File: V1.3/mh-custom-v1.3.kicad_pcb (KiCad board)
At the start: 2 copper layers, 93 x 91.3 mm, 118 parts, among them J1 Conn_01x03_Male, J10 Screw_Terminal_01x02, J11 Screw_Terminal_01x02, J12 Screw_Terminal_01x02, J13 USB_A, J14 Screw_Terminal_01x02, J15 Conn_02x16_Row_Letter_Last, J16 Conn_02x12_Row_Letter_Last, J5 Screw_Terminal_01x02, J6 Screw_Terminal_01x02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

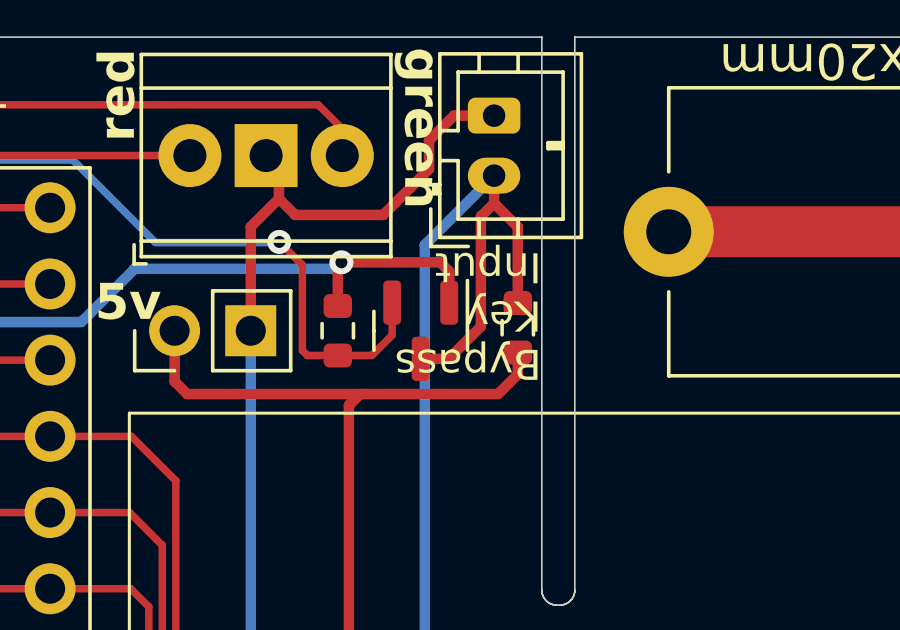
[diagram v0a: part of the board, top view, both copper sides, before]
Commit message: moved bypass key and led labels
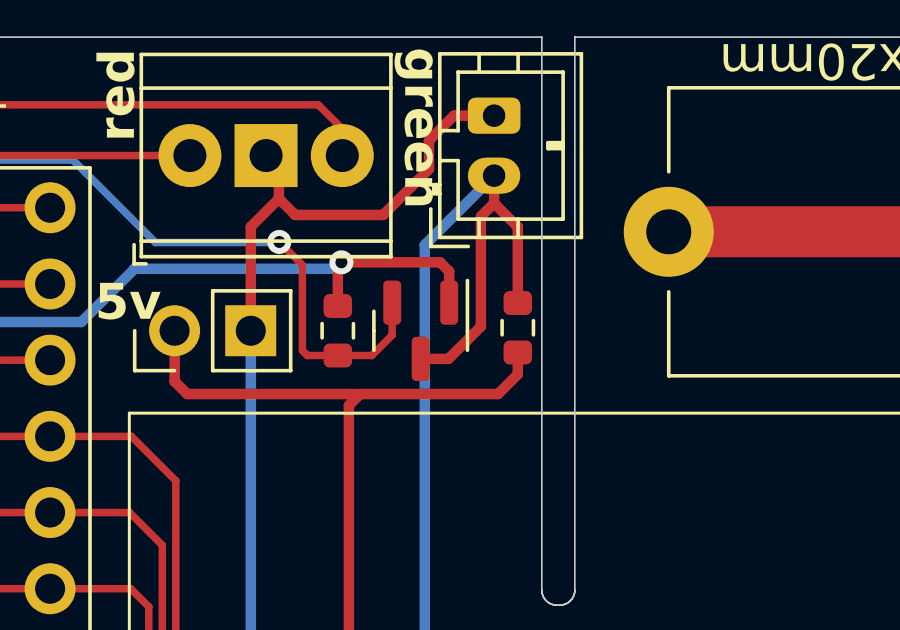
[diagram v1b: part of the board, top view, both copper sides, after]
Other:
- board text added: "R/G LED"
- board text added: "key"
- board text removed: "Bypass Key Input"
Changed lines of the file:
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@@
 		)
 	)
+	(gr_text "R/G LED"
+		(at 67.695 25.42 0)
+		(layer "B.SilkS")
+		(effects
+			(font
+				(size 1.5 1.5)
+				(thickness 0.3)
+				(bold yes)
+			)
+			(justify left bottom)
+		)
+	)
+	(gr_text "key"
+		(at 79.435 27.33 90)
+		(layer "B.SilkS")
+		(effects
+			(font
+				(size 1.5 1.5)
+				(thickness 0.3)
+				(bold yes)
+			)
+			(justify left bottom)
+		)
+	)
 	(gr_text "3 stages of relays\nFeather [WiFi] microcontroller\n2x E-Stop Integration\nCurrent Sensor"
 		(at 76.015 74.49 90)
@@
 		)
 	)
-	(gr_text "Bypass\nKey\nInput"
-		(at 82.015 32.19 180)
-		(layer "F.SilkS")
-		(effects
-			(font
-				(size 1 1)
-				(thickness 0.15)
-			)
-			(justify left)
-		)
-	)
 	(gr_text "MAX4A Fuses   5x20mm"
 		(at 97.935 23.7 180)
@@
 			"17958945-b4e5-4907-bdac-17ac1be8aeb7" "1eba8193-458a-4f8f-b496-5cd575e28d2e"
 			"21afb476-0163-4237-92db-8edd745e1eea" "22f72e0e-eb98-4883-b6db-5a118503c105"
-			"2550d0ec-683d-4be2-8794-d12b50d0d337" "29513e16-f12e-4352-b04b-dbd367b3c74a"
-			"295b06c7-e252-49b7-8a38-90fc508759aa" "34e09b9a-b600-4ada-8310-7c22730c7a67"
-			"38bfa293-1efc-4a4b-af5c-c6b398314e59" "3aa51f6b-5cfb-430a-a636-70ef1de7403d"
-			"3af1d50f-77a8-4823-b4be-9f8b6ecbdc7f" "3b67650f-9d43-435d-a4cb-f2b5c7b001b8"
-			"3e743c7e-5ef6-4c2b-9c4e-ca277ca6c139" "408bff59-9e59-4f04-9da1-94cdd9e4103e"
-			"414d6d0b-ebf2-4fe3-8636-3efca53d629c" "439b5404-ade4-4f5e-b38e-8e408305b0c5"
-			"465002d1-5889-45b8-a6e7-8e887e534c1e" "492cf508-daab-4356-a38d-12ad1886da1f"
-			"50597134-2ed5-408f-a813-e2581a61d251" "5698626b-8952-45af-bb77-57279943d3eb"
-			"584212ba-44d1-45a4-bfd9-fdcf5eec124d" "590466cf-07d7-4fb1-b0d5-cbfa69c59bae"
-			"59d04f74-5c65-460f-b996-c2b3a4ebb9fb" "5a2e864c-16e6-40d4-acce-bcec9eb9347b"
-			"5b481577-4d0c-4c9c-b396-abc133042409" "6134f302-f9a9-4cd2-8eea-1ba168d35a78"
-			"62588a2d-fa92-4e05-ae38-b68466984832" "6c0ca485-d34e-470e-98bc-fbc74fdcb446"
-			"70326d7e-9b73-4430-bb83-f5fa03c84a4d" "73fe44ca-7166-4dc6-a87e-0772ad8112bc"
-			"78a1b218-8262-40ce-b14f-864e02ac2a92" "82d2c86b-827d-4dae-b0b6-12a0a6e95fc4"
-			"84ab4415-58b5-44fc-a97a-9d447aef33e6" "85f53170-4516-4501-a000-3ba7a9aff425"
-			"87784ff4-fb95-4a61-8c16-4d3351d61679" "8d47d5ad-25f9-428f-900d-75f7e963e3c9"
-			"8e117e59-b2e0-4634-bd48-d223e300b05c" "8eb8abda-5f0b-480b-b9fa-d0bf0bbb88cf"
-			"934da9de-7ab7-41db-b04a-0737f17e9c00" "94d803e1-8cde-45aa-a1dc-5da856157556"
-			"97b0d988-ae48-44f6-b5d7-e3019f3f0008" "9c4cb01b-a57f-45d4-acdb-abd029d172c6"
-			"9d02bc0a-ac59-4ac8-ba2a-c8af13b700e9" "9f149bd0-1082-4a7f-8192-95bd0183291d"
-			"a360a2a5-503b-4e7b-ade7-c66933740494" "a3e29f78-74de-4864-8898-e08405603c39"
-			"a9a19ec2-157e-4fee-91ac-d43c3b62c388" "acae978b-2fc8-4245-a42c-13c7bcd02ae8"
-			"af898ec6-8398-41a1-b0ba-9b606ce959ce" "b1318dab-5955-43c4-ac8c-b5a328f70a44"
-			"b2d13ab4-6efe-4b38-9b5b-f173cdfb8701" "b42c07d1-11fe-4424-b759-0d1276d03285"
-			"b6e41199-3fee-4d47-bd67-1ba33aa292e9" "b925d684-2c76-4e7a-b534-ac7c16bc0ae3"
-			"bc5ed0a8-de7a-4749-a68e-229cd1c0a231" "c1ba262e-6206-4bc8-a9ac-dae23533be60"
-			"c2ac6580-32b8-4e11-a545-ebc8dc801088" "c7707fc4-b28a-4655-8f75-10bdcb199e59"
-			"ca6a5f29-a8e5-45c1-ae70-af50c3a38a07" "cc2fcf3c-85e7-49be-b7bd-3e4b750f2179"
-			"ce898617-f0af-4fd4-b81a-07bd27980ecc" "cf8372bf-3328-4e25-9cf9-8e29cff3b115"
-			"d2b5cae1-5983-4108-8894-ccd4c23e48ee" "d505db84-2666-403b-9e6f-7135ce8c6eaa"
-			"e5543da5-a531-4810-83b5-3e0106f3a2cc" "e56ba5bc-d532-4dd0-a4c4-5f68e814dbc5"
-			"e670ab2b-b84d-45d7-bd66-d3d1c50571f3" "ead11c8b-1ad6-4648-827c-de4dfb5421bd"
-			"edf3f12c-61c8-467c-8d0e-44c0f2bdbe4d" "f7141665-cc66-4778-895e-a5e442e220fc"
-			"fb9e3b5e-7543-43c4-87dc-00f8ad6d4efc" "fd1a9feb-2a32-421e-b513-64c14429d371"
+			"2550d0ec-683d-4be2-8794-d12b50d0d337" "295b06c7-e252-49b7-8a38-90fc508759aa"
+			"34e09b9a-b600-4ada-8310-7c22730c7a67" "38bfa293-1efc-4a4b-af5c-c6b398314e59"
+			"3aa51f6b-5cfb-430a-a636-70ef1de7403d" "3af1d50f-77a8-4823-b4be-9f8b6ecbdc7f"
+			"3b67650f-9d43-435d-a4cb-f2b5c7b001b8" "3e743c7e-5ef6-4c2b-9c4e-ca277ca6c139"
+			"408bff59-9e59-4f04-9da1-94cdd9e4103e" "414d6d0b-ebf2-4fe3-8636-3efca53d629c"
+			"439b5404-ade4-4f5e-b38e-8e408305b0c5" "465002d1-5889-45b8-a6e7-8e887e534c1e"
+			"492cf508-daab-4356-a38d-12ad1886da1f" "50597134-2ed5-408f-a813-e2581a61d251"
+			"5698626b-8952-45af-bb77-57279943d3eb" "584212ba-44d1-45a4-bfd9-fdcf5eec124d"
+			"590466cf-07d7-4fb1-b0d5-cbfa69c59bae" "59d04f74-5c65-460f-b996-c2b3a4ebb9fb"
+			"5a2e864c-16e6-40d4-acce-bcec9eb9347b" "5b481577-4d0c-4c9c-b396-abc133042409"
+			"6134f302-f9a9-4cd2-8eea-1ba168d35a78" "62588a2d-fa92-4e05-ae38-b68466984832"
+			"6c0ca485-d34e-470e-98bc-fbc74fdcb446" "70326d7e-9b73-4430-bb83-f5fa03c84a4d"
+			"73fe44ca-7166-4dc6-a87e-0772ad8112bc" "78a1b218-8262-40ce-b14f-864e02ac2a92"
+			"82d2c86b-827d-4dae-b0b6-12a0a6e95fc4" "84ab4415-58b5-44fc-a97a-9d447aef33e6"
+			"85f53170-4516-4501-a000-3ba7a9aff425" "87784ff4-fb95-4a61-8c16-4d3351d61679"
+			"8d47d5ad-25f9-428f-900d-75f7e963e3c9" "8e117e59-b2e0-4634-bd48-d223e300b05c"
+			"8eb8abda-5f0b-480b-b9fa-d0bf0bbb88cf" "934da9de-7ab7-41db-b04a-0737f17e9c00"
+			"94d803e1-8cde-45aa-a1dc-5da856157556" "97b0d988-ae48-44f6-b5d7-e3019f3f0008"
+			"9c4cb01b-a57f-45d4-acdb-abd029d172c6" "9d02bc0a-ac59-4ac8-ba2a-c8af13b700e9"
+			"9f149bd0-1082-4a7f-8192-95bd0183291d" "a360a2a5-503b-4e7b-ade7-c66933740494"
+			"a3e29f78-74de-4864-8898-e08405603c39" "a9a19ec2-157e-4fee-91ac-d43c3b62c388"
+			"acae978b-2fc8-4245-a42c-13c7bcd02ae8" "af898ec6-8398-41a1-b0ba-9b606ce959ce"
+			"b1318dab-5955-43c4-ac8c-b5a328f70a44" "b2d13ab4-6efe-4b38-9b5b-f173cdfb8701"
+			"b42c07d1-11fe-4424-b759-0d1276d03285" "b6e41199-3fee-4d47-bd67-1ba33aa292e9"
+			"b925d684-2c76-4e7a-b534-ac7c16bc0ae3" "bc5ed0a8-de7a-4749-a68e-229cd1c0a231"
+			"c1ba262e-6206-4bc8-a9ac-dae23533be60" "c2ac6580-32b8-4e11-a545-ebc8dc801088"
+			"c7707fc4-b28a-4655-8f75-10bdcb199e59" "ca6a5f29-a8e5-45c1-ae70-af50c3a38a07"
+			"cc2fcf3c-85e7-49be-b7bd-3e4b750f2179" "ce898617-f0af-4fd4-b81a-07bd27980ecc"
+			"cf8372bf-3328-4e25-9cf9-8e29cff3b115" "d2b5cae1-5983-4108-8894-ccd4c23e48ee"
+			"d505db84-2666-403b-9e6f-7135ce8c6eaa" "e5543da5-a531-4810-83b5-3e0106f3a2cc"
+			"e56ba5bc-d532-4dd0-a4c4-5f68e814dbc5" "e670ab2b-b84d-45d7-bd66-d3d1c50571f3"
+			"ead11c8b-1ad6-4648-827c-de4dfb5421bd" "edf3f12c-61c8-467c-8d0e-44c0f2bdbe4d"
+			"f7141665-cc66-4778-895e-a5e442e220fc" "fb9e3b5e-7543-43c4-87dc-00f8ad6d4efc"
+			"fd1a9feb-2a32-421e-b513-64c14429d371"
 		)
 	)

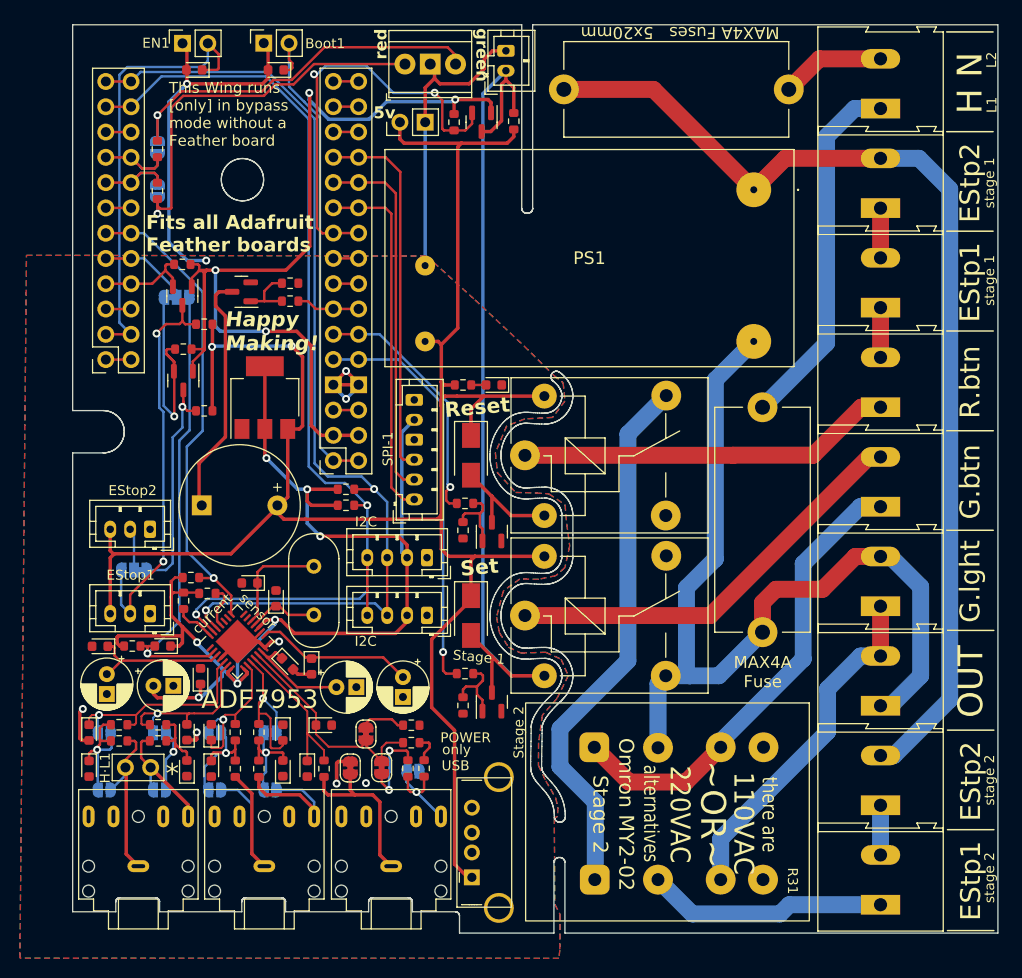
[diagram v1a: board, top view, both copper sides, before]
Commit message: rounded high voltage tracks
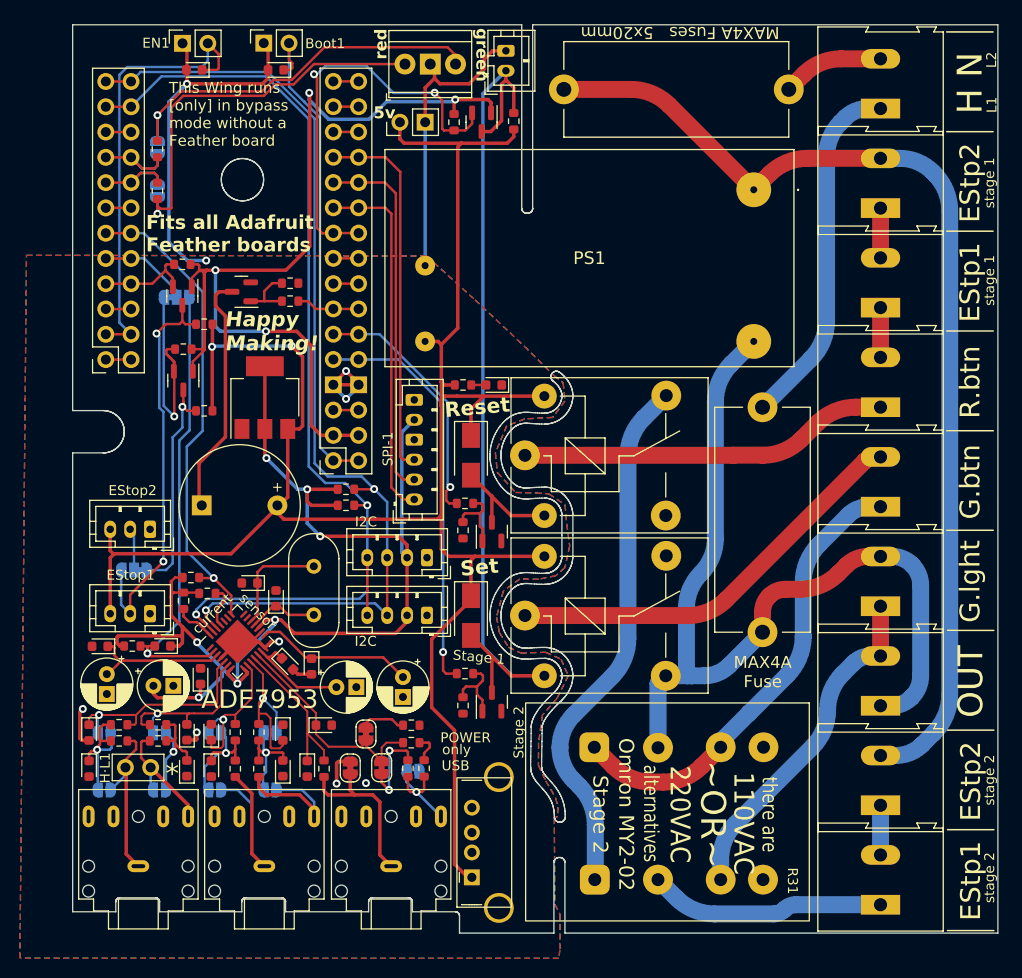
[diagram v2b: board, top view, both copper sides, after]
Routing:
- net reset: track 54.5 -> 53.3 mm
- net Member-Green-Button-2: track 47.6 -> 46.6 mm
- net Green-Indicator-light-2: track 35.3 -> 34.4 mm
- net H/L1: track 36.5 -> 35.8 mm
- net Member-Red-Reset-Button-1: track 37.7 -> 37.2 mm

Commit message: revised some values for interactive BOM
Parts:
- IN-1: value H/L1 -> 3.5mm
- IN-2: value N/L2 -> 3.5mm
- IN-3: value VOLTS -> 3.5mm
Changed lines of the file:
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@@
 			)
 		)
-		(property "Value" "H/L1"
+		(property "Value" "3.5mm"
 			(at 0 -10 0)
 			(layer "F.Fab")
@@
 			)
 		)
-		(property "Value" "N/L2"
+		(property "Value" "3.5mm"
 			(at 0 -10 0)
 			(layer "F.Fab")
@@
 			)
 		)
-		(property "Value" "VOLTS"
+		(property "Value" "3.5mm"
 			(at 0 -10 0)
 			(layer "F.Fab")

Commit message: added interactive Bill of Materials
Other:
- board text added: "5V"
- board text added: "GND"
- board text added: "Use at own risk"
- board text added: "bypass key"
- board text added: "grn"
- board text added: "https://learn.adafruit.com/ adafruit-feather/feather-specification"
- board text added: "status LEDs"
- board text removed: "R/G LED"
- board text removed: "Use at your own risk"
- board text removed: "key"
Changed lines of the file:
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@@
 		(legacy_teardrops no)
 	)
-	(paper "A4")
+	(paper "USLetter")
+	(title_block
+		(title "Cardsystem Combined-Use Feather Wing")
+		(date "2024-03-02")
+		(rev "1.3.1")
+		(company "MakeHaven")
+		(comment 1 "Feather Wing compatable Board")
+		(comment 2 "Primary use: tool control & RFID card reader")
+		(comment 3 "Tool control by onboard multi-stage Relays - powered by input AC voltage")
+		(comment 4 "Add daughter board for RFID card read: I2C intended, but SPI could work as well")
+		(comment 5 "other extensions possible, as specified in Docs")
+	)
 	(layers
 		(0 "F.Cu" signal)
@@
 		(layer "B.SilkS")
 	)
+	(gr_line
+		(start 74.325 33.87)
+		(end 67.705 33.87)
+		(stroke
+			(width 0.15)
+			(type default)
+		)
+		(layer "B.SilkS")
+	)
 	(gr_poly
 		(pts
@@
 		(layer "B.SilkS")
 	)
+	(gr_line
+		(start 74.325 30.55)
+		(end 74.325 33.87)
+		(stroke
+			(width 0.15)
+			(type default)
+		)
+		(layer "B.SilkS")
+	)
 	(gr_poly
 		(pts
@@
 		(layer "B.SilkS")
 	)
+	(gr_line
+		(start 74.325 30.55)
+		(end 67.695 30.55)
+		(stroke
+			(width 0.15)
+			(type default)
+		)
+		(layer "B.SilkS")
+	)
 	(gr_poly
 		(pts
@@
 		(layer "B.SilkS")
 	)
+	(gr_line
+		(start 71.015 33.87)
+		(end 71.01 30.55)
+		(stroke
+			(width 0.15)
+			(type default)
+		)
+		(layer "B.SilkS")
+	)
 	(gr_poly
 		(pts
@@
 	)
 	(gr_line
-		(start 74.873116 30.402956)
-		(end 74.876884 46.197043)
+		(start 38.445 35.65)
+		(end 38.476884 47.517044)
 		(stroke
 			(width 0.15)
@@
 		(layer "B.SilkS")
 	)
+	(gr_line
+		(start 67.695 30.55)
+		(end 67.705 33.87)
+		(stroke
+			(width 0.15)
+			(type default)
+		)
+		(layer "B.SilkS")
+	)
 	(gr_poly
 		(pts
@@
 		)
 	)
-	(gr_text "Use at your own risk"
-		(at 74.175 38.15 90)
+	(gr_text "Use at own risk"
+		(at 37.756884 41.517044 90)
 		(layer "B.SilkS")
 		(effects
@@
 		)
 	)
-	(gr_text "R/G LED"
-		(at 67.695 25.42 0)
+	(gr_text "red"
+		(at 71.425 25.77 0)
 		(layer "B.SilkS")
 		(effects
 			(font
-				(size 1.5 1.5)
-				(thickness 0.3)
-				(bold yes)
+				(size 1 1)
+				(thickness 0.15)
 			)
-			(justify left bottom)
+			(justify left bottom mirror)
 		)
 	)
-	(gr_text "key"
-		(at 79.435 27.33 90)
+	(gr_text "bypass key"
+		(at 79.465 22.81 90)
 		(layer "B.SilkS")
 		(effects
 			(font
-				(size 1.5 1.5)
-				(thickness 0.3)
-				(bold yes)
+				(size 1 1)
+				(thickness 0.15)
 			)
-			(justify left bottom)
+			(justify left bottom mirror)
 		)
 	)
@@
 		)
 	)
+	(gr_text "https://learn.adafruit.com/\nadafruit-feather/feather-specification"
+		(at 78.335 31.75 90)
+		(layer "B.SilkS")
+		(effects
+			(font
+				(size 1 1)
+				(thickness 0.15)
+			)
+			(justify left bottom mirror)
+		)
+	)
 	(gr_text "Hardware:\n"
 		(at 81.925 94.8 90)
@@
 		)
 	)
+	(gr_text "GND"
+		(at 74.355 31.89 0)
+		(layer "B.SilkS")
+		(effects
+			(font
+				(size 1 1)
+				(thickness 0.15)
+			)
+			(justify left bottom mirror)
+		)
+	)
+	(gr_text "grn"
+		(at 76.755 25.67 0)
+		(layer "B.SilkS")
+		(effects
+			(font
+				(size 1 1)
+				(thickness 0.15)
+			)
+			(justify left bottom mirror)
+		)
+	)
+	(gr_text "status LEDs"
+		(at 77.225 29.47 0)
+		(layer "B.SilkS")
+		(effects
+			(font
+				(size 1 1)
+				(thickness 0.15)
+			)
+			(justify left bottom mirror)
+		)
+	)
 	(gr_text "Vincent, Lior,\nJ.R., \nChris,\n& Ashley"
 		(at 61.575 38.4 0)
@@
 	)
 	(gr_text "makehaven.org/openshop"
-		(at 68.225 53.5 90)
+		(at 68.255 53.48 90)
 		(layer "B.SilkS")
 		(effects
 			(font
 				(size 2 2)
-				(thickness 0.4)
+				(thickness 0.25)
 			)
 			(justify mirror)
 		)
 	)
-	(gr_text "Keep fingers out of \nHigh Voltage Area"
-		(at 78.275 28.25 90)
+	(gr_text "Keep fingers out of High Voltage Area"
+		(at 80.815 28.99 90)
 		(layer "B.SilkS")
 		(effects
 			(font
-				(size 2 2)
-				(thickness 0.3)
+				(size 1.2 1.1)
+				(thickness 0.2)
 			)
 			(justify left mirror)
 		)
 	)
+	(gr_text "5V"
+		(at 69.735 32.01 0)
+		(layer "B.SilkS")
+		(effects
+			(font
+				(size 1 1)
+				(thickness 0.15)
+			)
+			(justify left bottom mirror)
+		)
+	)

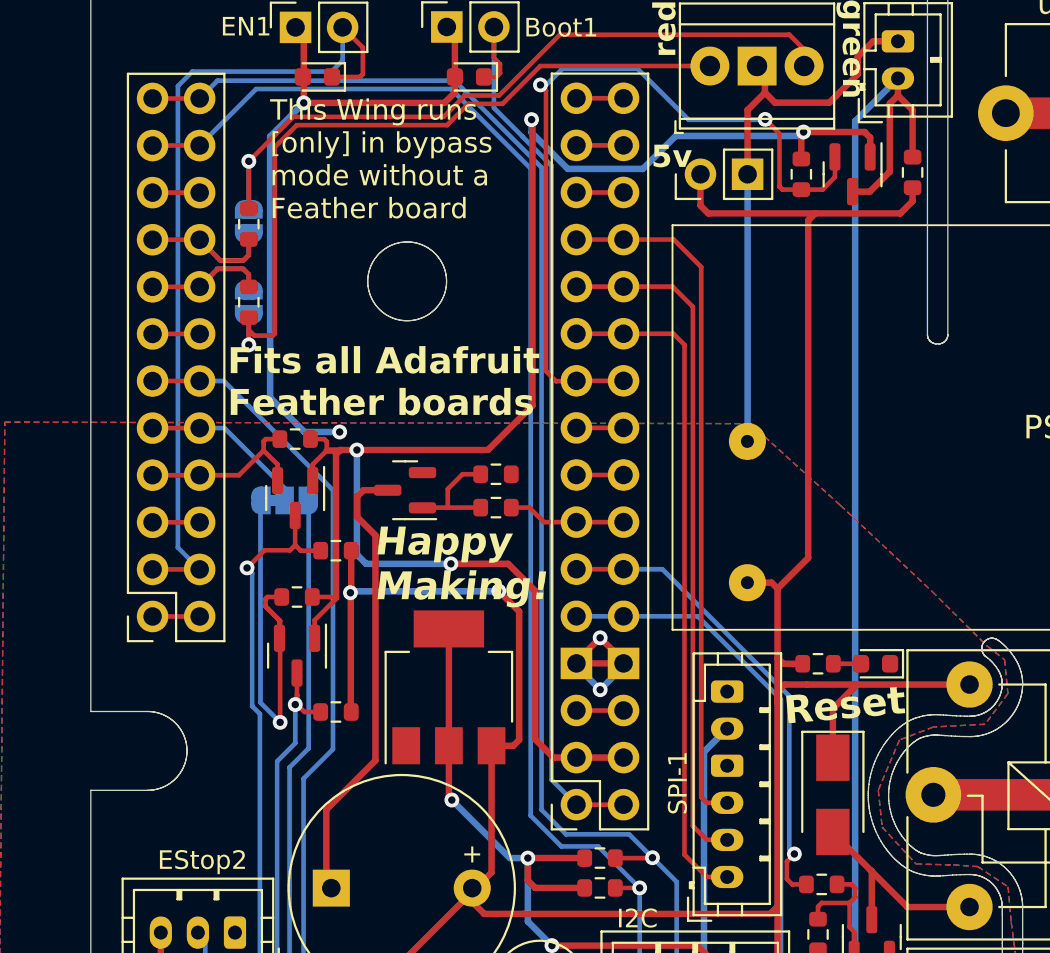
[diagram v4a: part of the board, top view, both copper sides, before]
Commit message: adjust silkscreen
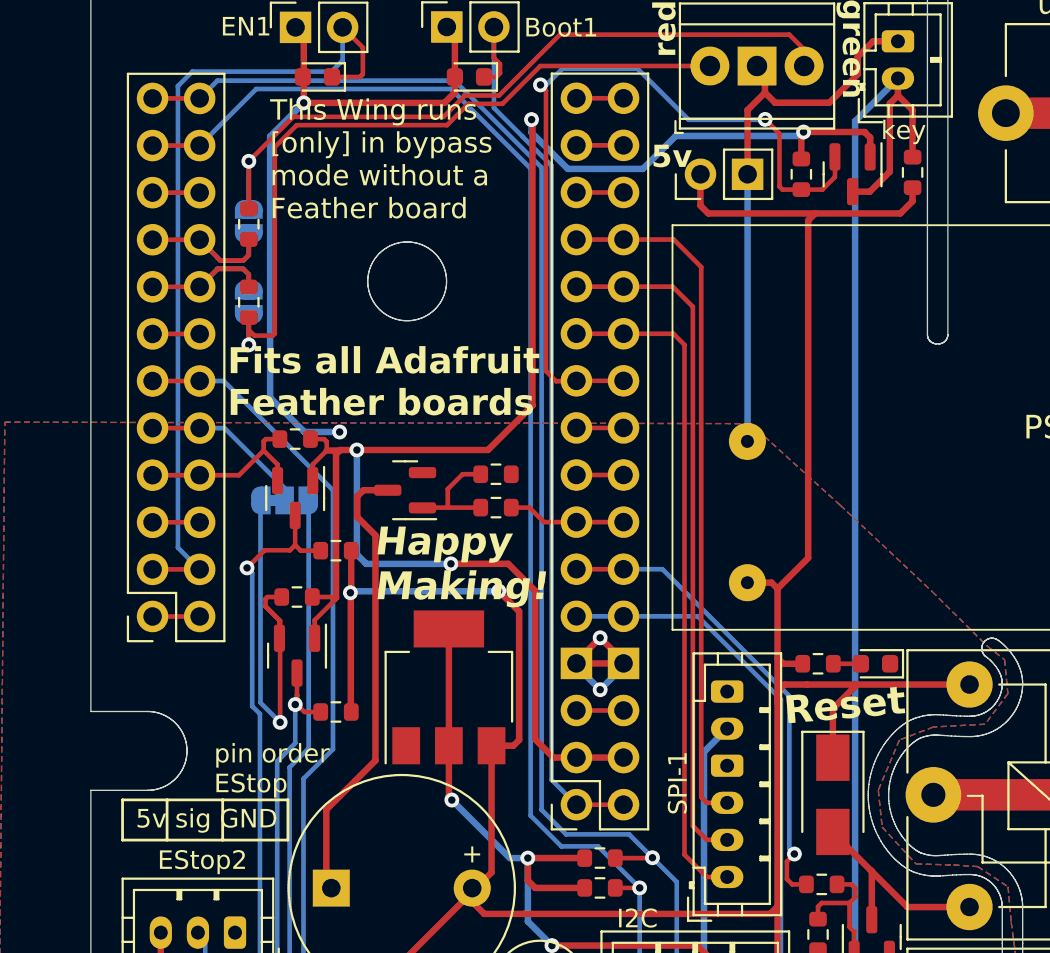
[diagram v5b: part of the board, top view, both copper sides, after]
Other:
- board text added: "5v sig GND"
- board text added: "key"
- board text added: "pin order EStop"
